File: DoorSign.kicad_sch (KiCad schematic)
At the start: 38 parts, among them J1 Wall, J2 Taster, J3 Taster-LED, U1 Pico, U2 PC817, U3 LM2575-5.0BT

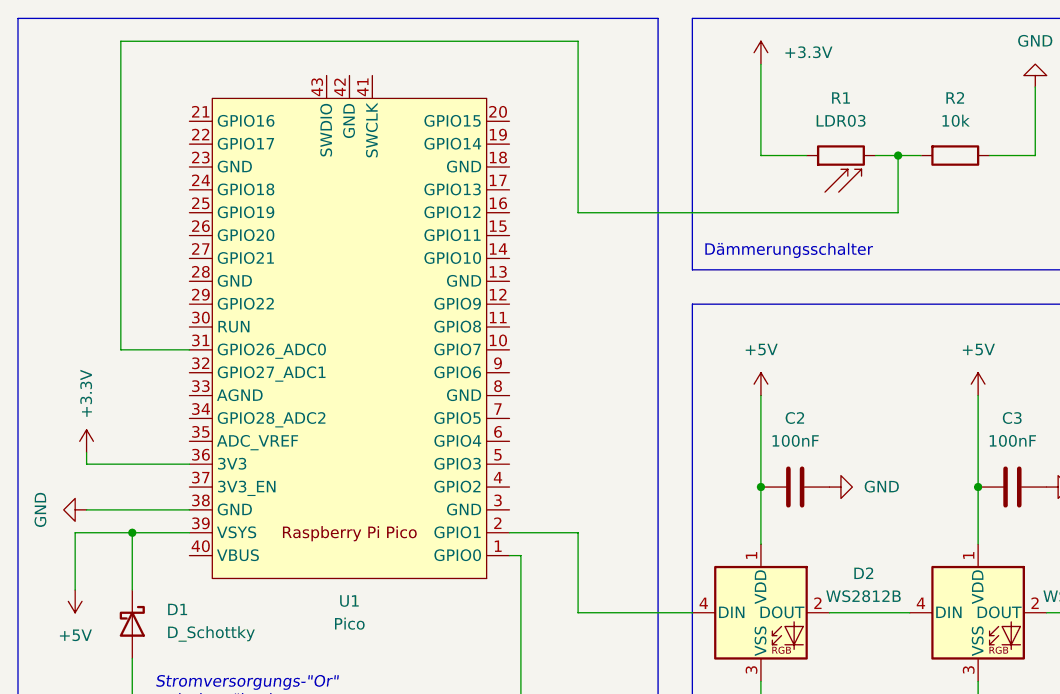
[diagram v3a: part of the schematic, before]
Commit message: connected all GND pins on the Pico
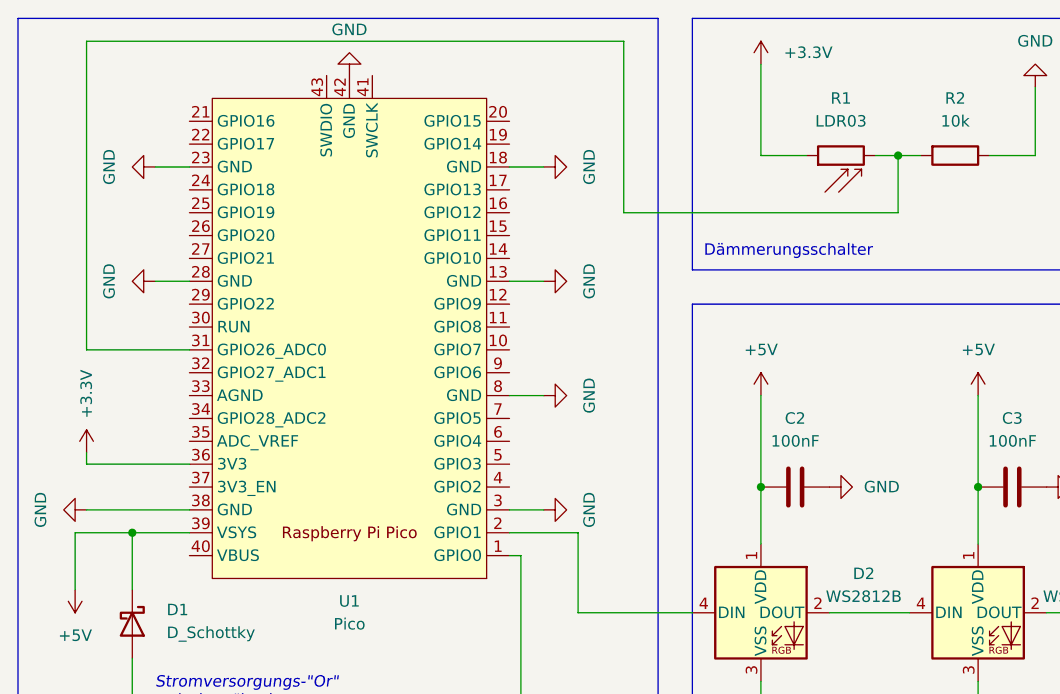
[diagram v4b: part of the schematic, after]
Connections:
- net GND: now also U1.13 (GND), U1.18 (GND), U1.23 (GND), U1.28 (GND), U1.3 (GND), U1.42 (GND), U1.8 (GND)
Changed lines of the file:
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@@
     (stroke (width 0) (type default) (color 0 0 0 0))
   )
-  (wire (pts (xy 25.4 19.05) (xy 25.4 53.34))
+  (wire (pts (xy 21.59 19.05) (xy 21.59 53.34))
     (stroke (width 0) (type default) (color 0 0 0 0))
   )
@@
     (stroke (width 0) (type default) (color 0 0 0 0))
   )
+  (wire (pts (xy 68.58 45.72) (xy 72.39 45.72))
+    (stroke (width 0) (type default) (color 0 0 0 0))
+  )
   (wire (pts (xy 128.27 82.55) (xy 137.16 82.55))
     (stroke (width 0) (type default) (color 0 0 0 0))
@@
     (stroke (width 0) (type default) (color 0 0 0 0))
   )
+  (wire (pts (xy 68.58 58.42) (xy 72.39 58.42))
+    (stroke (width 0) (type default) (color 0 0 0 0))
+  )
   (wire (pts (xy 241.3 68.58) (xy 241.3 74.93))
     (stroke (width 0) (type default) (color 0 0 0 0))
@@
     (stroke (width 0) (type default) (color 0 0 0 0))
   )
+  (wire (pts (xy 68.58 71.12) (xy 72.39 71.12))
+    (stroke (width 0) (type default) (color 0 0 0 0))
+  )
   (wire (pts (xy 168.91 58.42) (xy 168.91 68.58))
     (stroke (width 0) (type default) (color 0 0 0 0))
@@
     (stroke (width 0) (type default) (color 0 0 0 0))
   )
+  (wire (pts (xy 29.21 45.72) (xy 33.02 45.72))
+    (stroke (width 0) (type default) (color 0 0 0 0))
+  )
   (wire (pts (xy 80.01 142.24) (xy 80.01 143.51))
     (stroke (width 0) (type default) (color 0 0 0 0))
@@
     (stroke (width 0) (type default) (color 0 0 0 0))
   )
-  (wire (pts (xy 76.2 19.05) (xy 25.4 19.05))
+  (wire (pts (xy 81.28 19.05) (xy 21.59 19.05))
     (stroke (width 0) (type default) (color 0 0 0 0))
   )
@@
     (stroke (width 0) (type default) (color 0 0 0 0))
   )
+  (wire (pts (xy 29.21 33.02) (xy 33.02 33.02))
+    (stroke (width 0) (type default) (color 0 0 0 0))
+  )
   (wire (pts (xy 121.92 31.75) (xy 127 31.75))
     (stroke (width 0) (type default) (color 0 0 0 0))
@@
     (stroke (width 0) (type default) (color 0 0 0 0))
   )
+  (wire (pts (xy 68.58 33.02) (xy 72.39 33.02))
+    (stroke (width 0) (type default) (color 0 0 0 0))
+  )
   (wire (pts (xy 217.17 90.17) (xy 217.17 97.79))
     (stroke (width 0) (type default) (color 0 0 0 0))
@@
     (stroke (width 0) (type default) (color 0 0 0 0))
   )
-  (wire (pts (xy 76.2 38.1) (xy 76.2 19.05))
+  (wire (pts (xy 81.28 38.1) (xy 81.28 19.05))
     (stroke (width 0) (type default) (color 0 0 0 0))
   )
@@
     (stroke (width 0) (type default) (color 0 0 0 0))
   )
-  (wire (pts (xy 111.76 38.1) (xy 76.2 38.1))
+  (wire (pts (xy 111.76 38.1) (xy 81.28 38.1))
     (stroke (width 0) (type default) (color 0 0 0 0))
   )
@@
     (stroke (width 0) (type default) (color 0 0 0 0))
   )
-  (wire (pts (xy 25.4 53.34) (xy 33.02 53.34))
+  (wire (pts (xy 21.59 53.34) (xy 33.02 53.34))
     (stroke (width 0) (type default) (color 0 0 0 0))
   )
@@
     (pin "2")
   )
+  (symbol (lib_id "power:GND") (at 72.39 45.72 90) (unit 1)
+    (in_bom yes) (on_board yes)
+    (property "Reference" "#PWR0111" (id 0) (at 78.74 45.72 0)
+      (effects (font (size 1.27 1.27)) hide)
+    )
+    (property "Value" "GND" (id 1) (at 77.47 45.72 0))
+    (property "Footprint" "" (id 2) (at 72.39 45.72 0)
+      (effects (font (size 1.27 1.27)) hide)
+    )
+    (property "Datasheet" "" (id 3) (at 72.39 45.72 0)
+      (effects (font (size 1.27 1.27)) hide)
+    )
+    (pin "1")
+  )
+  (symbol (lib_id "power:GND") (at 29.21 33.02 270) (unit 1)
+    (in_bom yes) (on_board yes)
+    (property "Reference" "#PWR0108" (id 0) (at 22.86 33.02 0)
+      (effects (font (size 1.27 1.27)) hide)
+    )
+    (property "Value" "GND" (id 1) (at 24.13 33.02 0))
+    (property "Footprint" "" (id 2) (at 29.21 33.02 0)
+      (effects (font (size 1.27 1.27)) hide)
+    )
+    (property "Datasheet" "" (id 3) (at 29.21 33.02 0)
+      (effects (font (size 1.27 1.27)) hide)
+    )
+    (pin "1")
+  )
+  (symbol (lib_id "power:GND") (at 72.39 58.42 90) (unit 1)
+    (in_bom yes) (on_board yes)
+    (property "Reference" "#PWR0106" (id 0) (at 78.74 58.42 0)
+      (effects (font (size 1.27 1.27)) hide)
+    )
+    (property "Value" "GND" (id 1) (at 77.47 58.42 0))
+    (property "Footprint" "" (id 2) (at 72.39 58.42 0)
+      (effects (font (size 1.27 1.27)) hide)
+    )
+    (property "Datasheet" "" (id 3) (at 72.39 58.42 0)
+      (effects (font (size 1.27 1.27)) hide)
+    )
+    (pin "1")
+  )
   (symbol (lib_id "LED:WS2812B") (at 265.43 82.55 0) (unit 1)
     (in_bom yes) (on_board yes) (fields_autoplaced)
@@
     (pin "1")
   )
+  (symbol (lib_id "power:GND") (at 50.8 22.86 180) (unit 1)
+    (in_bom yes) (on_board yes)
+    (property "Reference" "#PWR0107" (id 0) (at 50.8 16.51 0)
+      (effects (font (size 1.27 1.27)) hide)
+    )
+    (property "Value" "GND" (id 1) (at 50.8 17.78 0))
+    (property "Footprint" "" (id 2) (at 50.8 22.86 0)
+      (effects (font (size 1.27 1.27)) hide)
+    )
+    (property "Datasheet" "" (id 3) (at 50.8 22.86 0)
+      (effects (font (size 1.27 1.27)) hide)
+    )
+    (pin "1")
+  )
   (symbol (lib_id "Diode:1N4001") (at 116.84 189.23 180) (unit 1)
     (in_bom yes) (on_board yes) (fields_autoplaced)
@@
     (pin "1")
     (pin "2")
+  )
+  (symbol (lib_id "power:GND") (at 29.21 45.72 270) (unit 1)
+    (in_bom yes) (on_board yes)
+    (property "Reference" "#PWR0109" (id 0) (at 22.86 45.72 0)
+      (effects (font (size 1.27 1.27)) hide)
+    )
+    (property "Value" "GND" (id 1) (at 24.13 45.72 0))
+    (property "Footprint" "" (id 2) (at 29.21 45.72 0)
+      (effects (font (size 1.27 1.27)) hide)
+    )
+    (property "Datasheet" "" (id 3) (at 29.21 45.72 0)
+      (effects (font (size 1.27 1.27)) hide)
+    )
+    (pin "1")
   )
   (symbol (lib_id "Device:C") (at 100.33 68.58 270) (unit 1)
@@
     (pin "5")
   )
+  (symbol (lib_id "power:GND") (at 72.39 33.02 90) (unit 1)
+    (in_bom yes) (on_board yes)
+    (property "Reference" "#PWR0110" (id 0) (at 78.74 33.02 0)
+      (effects (font (size 1.27 1.27)) hide)
+    )
+    (property "Value" "GND" (id 1) (at 77.47 33.02 0))
+    (property "Footprint" "" (id 2) (at 72.39 33.02 0)
+      (effects (font (size 1.27 1.27)) hide)
+    )
+    (property "Datasheet" "" (id 3) (at 72.39 33.02 0)
+      (effects (font (size 1.27 1.27)) hide)
+    )
+    (pin "1")
+  )
   (symbol (lib_id "power:GND") (at 59.69 162.56 180) (unit 1)
     (in_bom yes) (on_board yes) (fields_autoplaced)
@@
     (pin "1")
     (pin "2")
+  )
+  (symbol (lib_id "power:GND") (at 72.39 71.12 90) (unit 1)
+    (in_bom yes) (on_board yes)
+    (property "Reference" "#PWR0105" (id 0) (at 78.74 71.12 0)
+      (effects (font (size 1.27 1.27)) hide)
+    )
+    (property "Value" "GND" (id 1) (at 77.47 71.12 0))
+    (property "Footprint" "" (id 2) (at 72.39 71.12 0)
+      (effects (font (size 1.27 1.27)) hide)
+    )
+    (property "Datasheet" "" (id 3) (at 72.39 71.12 0)
+      (effects (font (size 1.27 1.27)) hide)
+    )
+    (pin "1")
   )
   (symbol (lib_id "Device:C") (at 245.11 68.58 270) (unit 1)
@@
       (reference "#PWR0104") (unit 1) (value "GND") (footprint "")
     )
+    (path "/eccd99ea-ae1b-4426-a313-ceef52838f2c"
+      (reference "#PWR0105") (unit 1) (value "GND") (footprint "")
+    )
+    (path "/2681dbd1-643b-4221-ad2d-d40ee8c83b5a"
+      (reference "#PWR0106") (unit 1) (value "GND") (footprint "")
+    )
+    (path "/6f534157-aa45-444c-b8a0-10f1131eabc5"
+      (reference "#PWR0107") (unit 1) (value "GND") (footprint "")
+    )
+    (path "/21bc3d61-e8a1-4643-9662-f3f8e59c380a"
+      (reference "#PWR0108") (unit 1) (value "GND") (footprint "")
+    )
+    (path "/7bce405a-91e5-4e0b-bd60-2850d6eebce9"
+      (reference "#PWR0109") (unit 1) (value "GND") (footprint "")
+    )
+    (path "/99f2757a-07ce-4048-918d-37f37be77055"
+      (reference "#PWR0110") (unit 1) (value "GND") (footprint "")
+    )
+    (path "/219036a8-88ec-40be-a14b-e0ddbc78bf19"
+      (reference "#PWR0111") (unit 1) (value "GND") (footprint "")
+    )
     (path "/49927729-dc2e-4ac4-b7aa-0e4f2f15cd80"
